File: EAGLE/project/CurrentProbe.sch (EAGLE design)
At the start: 55 parts, among them IC1 MC7805CTG, J1 227161-1, J2 ZX62WD1-B-5PC, J3 OQ0232X1XXXXG, J4 OQ0232X1XXXXG, J5 OQ0232X1XXXXG, J6 CTB932HE/3, U1 CKSR_6-NP, U2 OPA206ADR, U3 ACS724LLCTR-5AB-T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

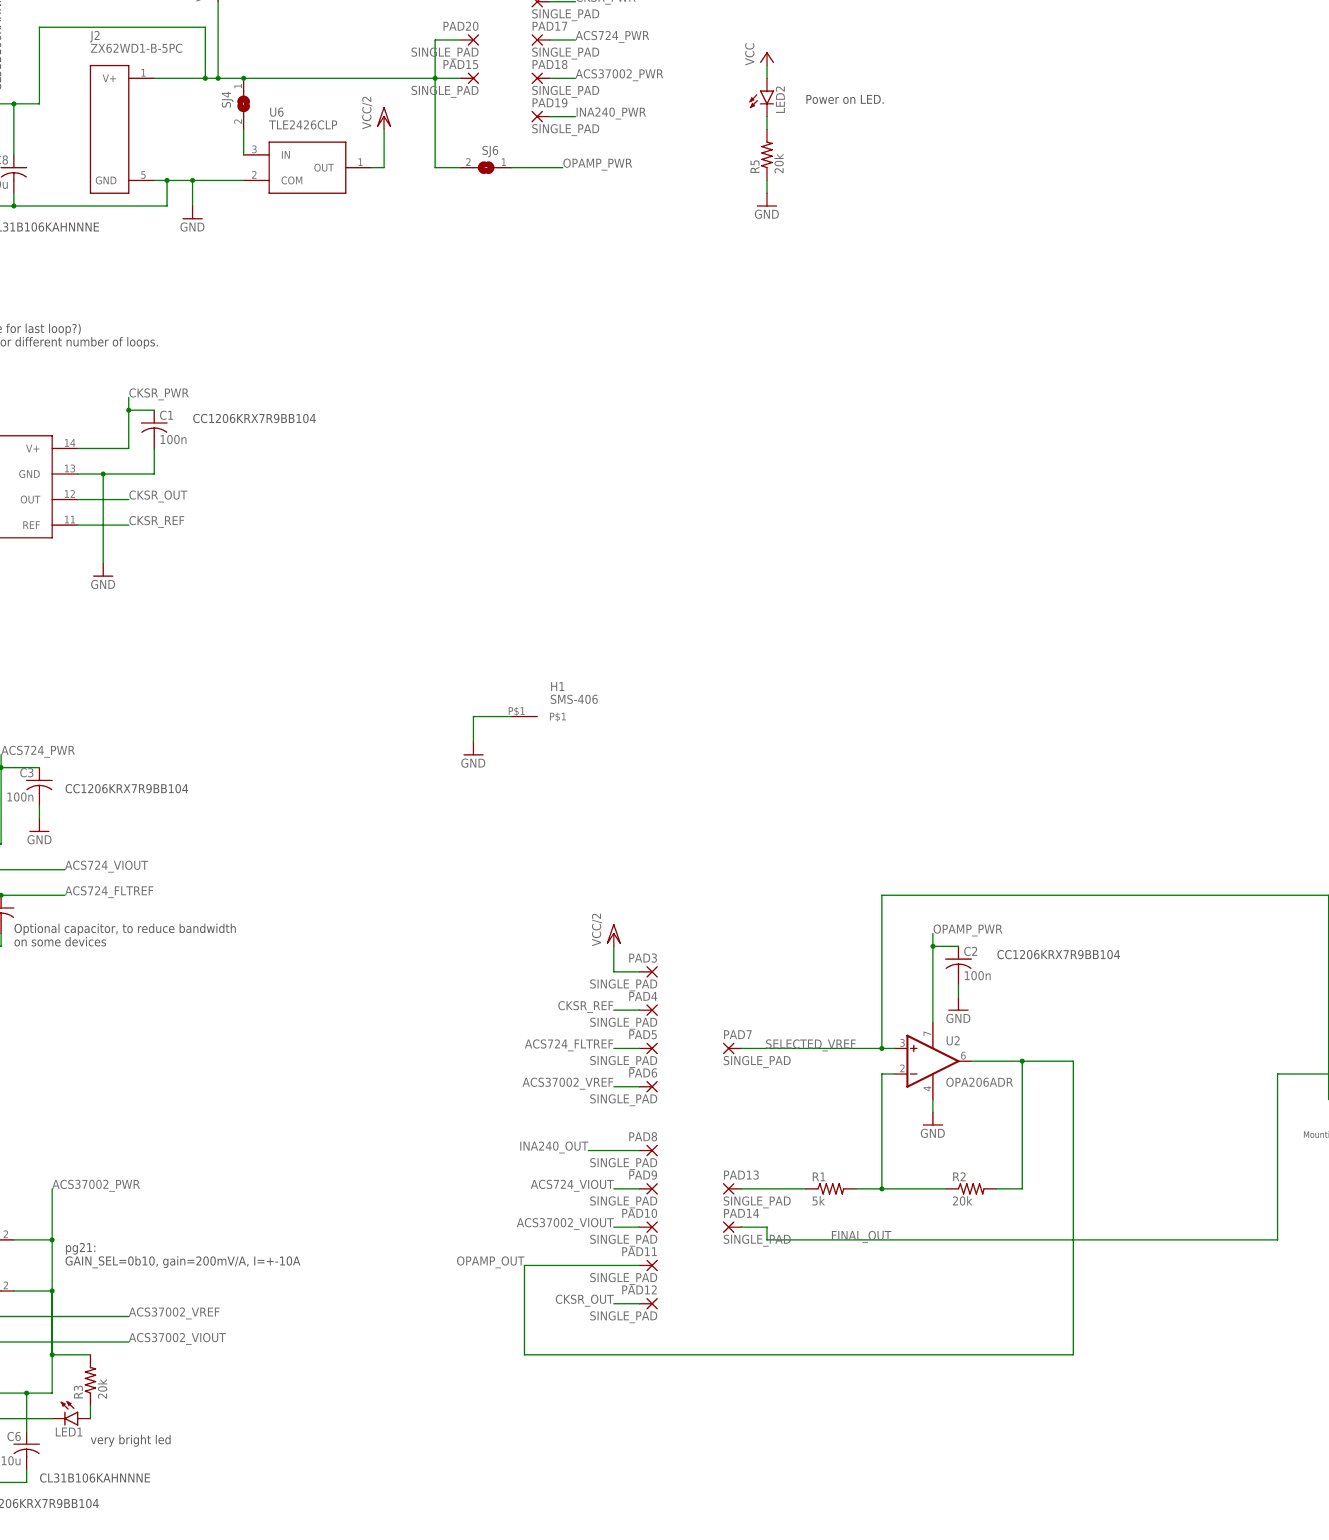
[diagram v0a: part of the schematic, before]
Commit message: Added more notes to schematic about jumper options. Added images.
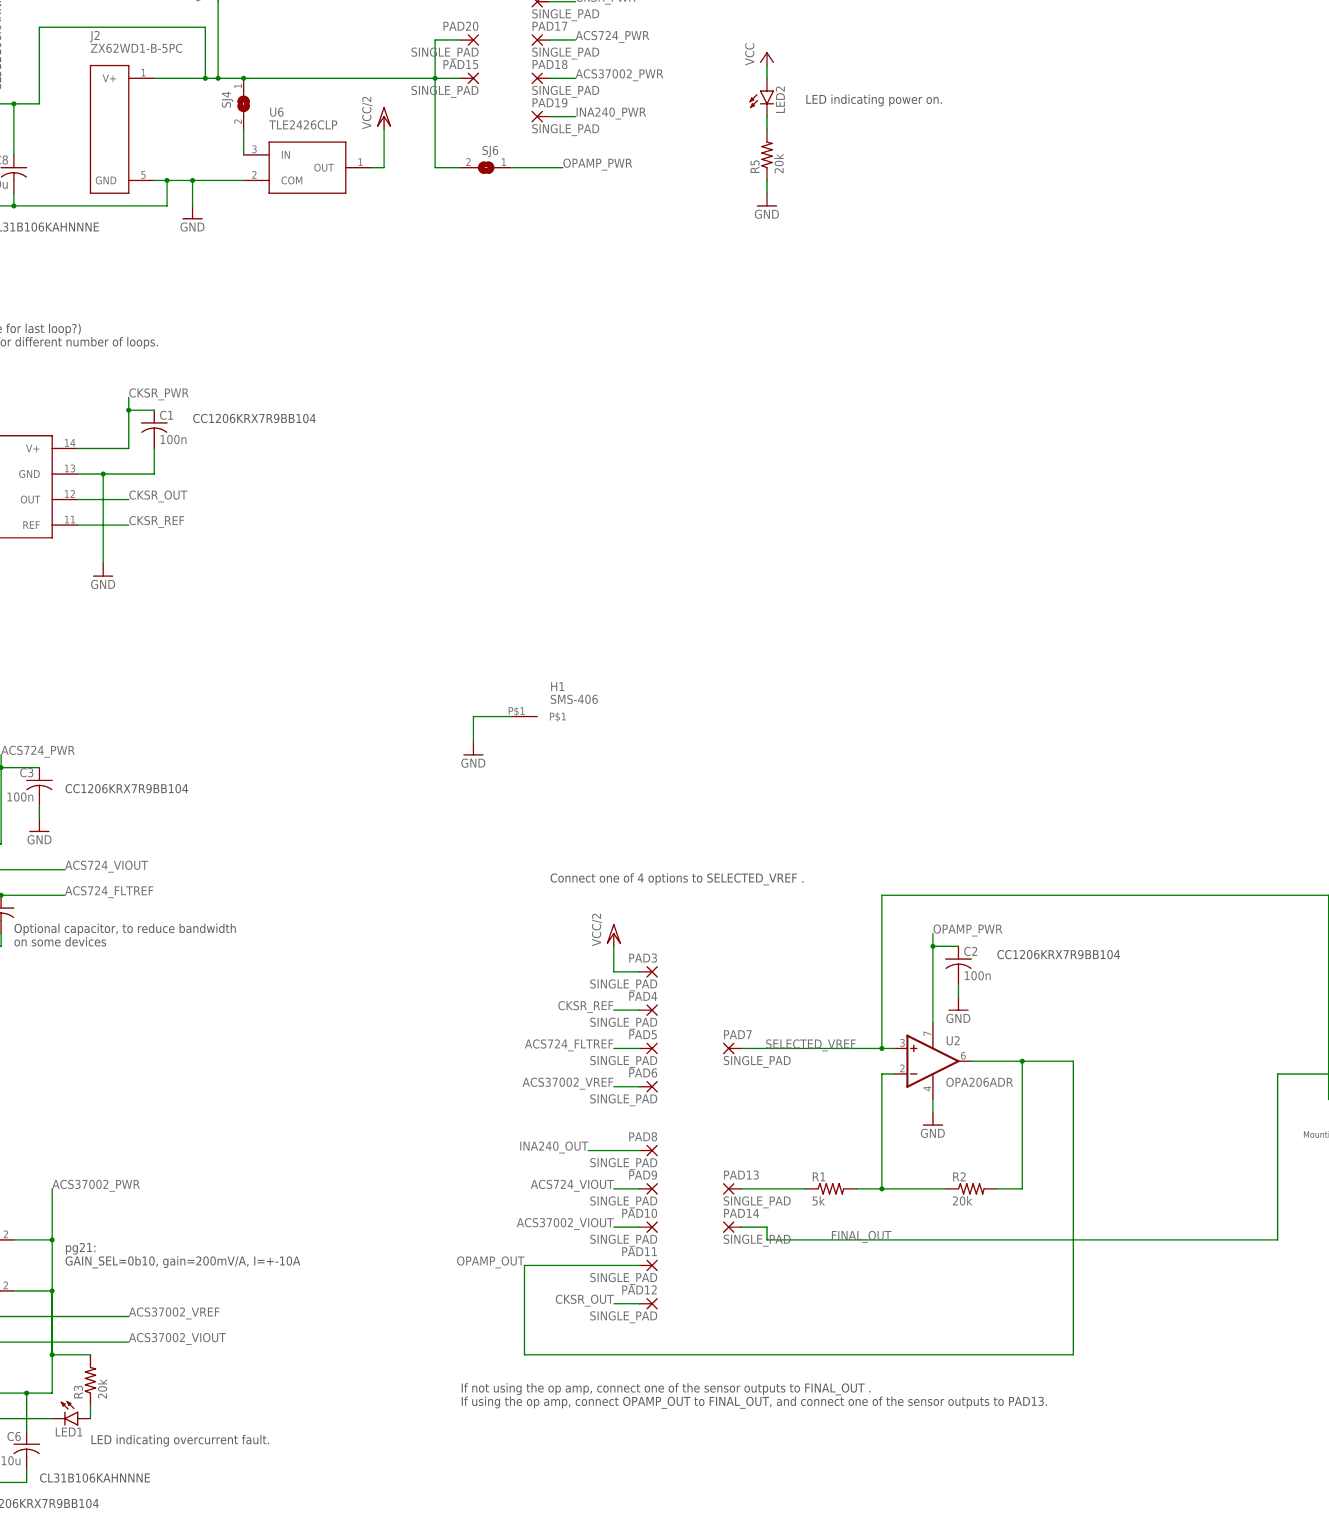
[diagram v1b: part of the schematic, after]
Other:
- note added: "Connect one of 4 options to SELECTED_VREF ."
- note added: "If not using the op amp, connect one of the sensor outputs to FINAL_OUT . If using the op amp, connect OPAMP_OUT to FINAL_OUT, and connect one of the sensor outputs to PAD13."
- note added: "LED indicating overcurrent fault."
- note added: "LED indicating power on."
- note removed: "Power on LED."
- note removed: "very bright led"
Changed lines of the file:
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@@
 <text x="78.74" y="-111.76" size="1.778" layer="97">pg21:
 GAIN_SEL=0b10, gain=200mV/A, I=+-10A</text>
-<text x="83.82" y="-147.32" size="1.778" layer="97">very bright led</text>
+<text x="83.82" y="-147.32" size="1.778" layer="97">LED indicating overcurrent fault.</text>
 <text x="48.26" y="-248.92" size="1.778" layer="97">OR, AD8411AWBRZ</text>
 <text x="33.02" y="-205.74" size="1.778" layer="97" rot="R180">NCW0612MC1207FP500</text>
@@
 <text x="63.5" y="93.98" size="1.778" layer="97">CL31B106KAHNNNE</text>
 <text x="27.94" y="-226.06" size="1.778" layer="97">0.12 Ohm</text>
-<text x="226.06" y="119.38" size="1.778" layer="97">Power on LED.</text>
+<text x="226.06" y="119.38" size="1.778" layer="97">LED indicating power on.</text>
 <text x="93.98" y="-231.14" size="1.778" layer="97">SJ5#1 and SJ3#2 next to each other. May bridge.</text>
+<text x="175.26" y="-35.56" size="1.778" layer="97">Connect one of 4 options to SELECTED_VREF .</text>
+<text x="157.48" y="-139.7" size="1.778" layer="97">If not using the op amp, connect one of the sensor outputs to FINAL_OUT .
+If using the op amp, connect OPAMP_OUT to FINAL_OUT, and connect one of the sensor outputs to PAD13.</text>
 </plain>
 <instances>
